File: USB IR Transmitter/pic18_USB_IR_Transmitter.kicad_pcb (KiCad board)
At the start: 2 copper layers, 50.8 x 25.4 mm, 26 parts, among them CON1 USB-MINI-B, P1 CONN_6, P2 CONN_4, P3 CONN_6, P4 CONN_6, P5 CONN_4, P6 CONN_1, P7 CONN_8, Q1 2N7002, U1 1586-PIC18F4550-I/PT, X1 12Mhz

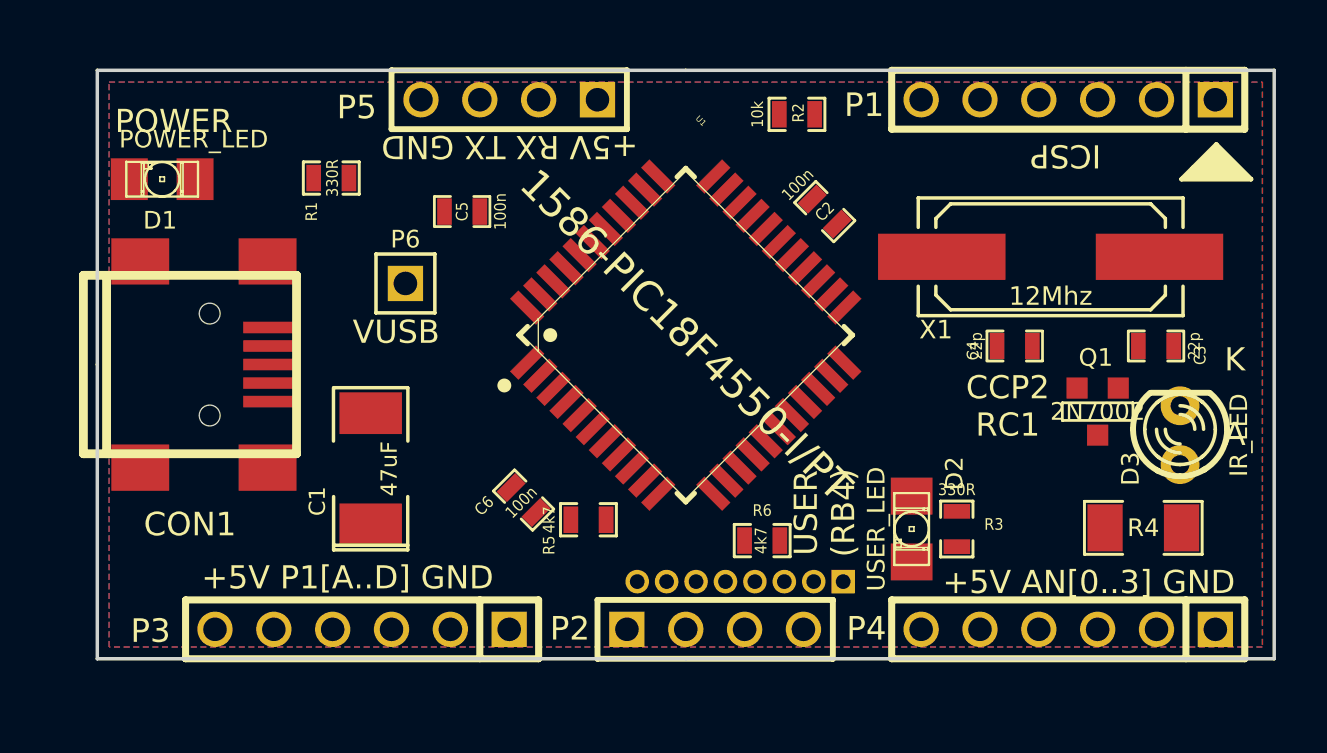
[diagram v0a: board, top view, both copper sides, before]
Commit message: fixed footprint name error in PIC18f board, rerouted board layout
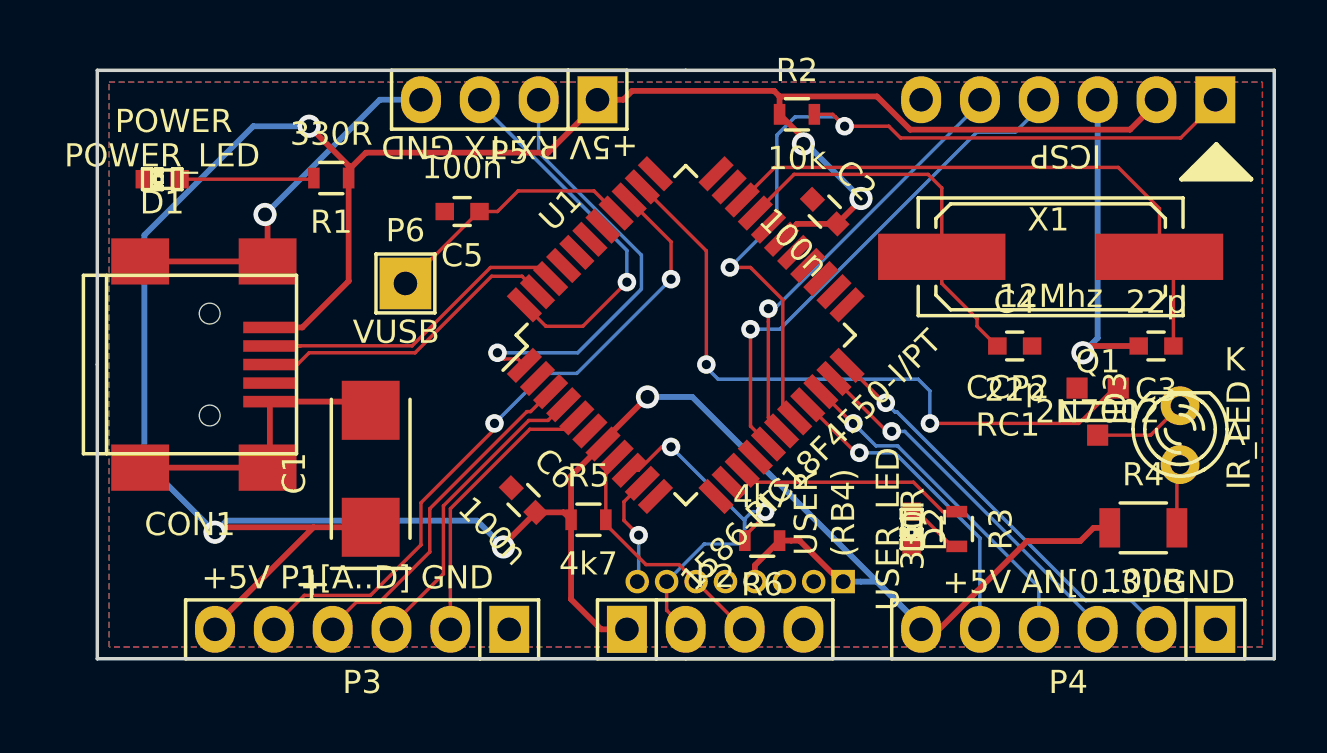
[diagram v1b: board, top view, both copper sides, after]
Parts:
- C1: footprint SM2010 -> Capacitors_Tantalum_SMD:TantalC_SizeC_EIA-6032_Reflow
- C2, C3, C4, C5, C6: footprint SM0603_Capa -> Capacitors_SMD:C_0603
- CON1: footprint USB_MINI_B -> Connect:USB_Mini-B
- D1, D2: footprint LED-1206 -> LEDs:LED-0603
- D3: footprint LED-3MM -> LEDs:LED-3MM
- P1: footprint PIN_ARRAY-6X1 -> Pin_Headers:Pin_Header_Angled_1x06; moved to B.Cu
- P2, P5: footprint PIN_ARRAY_4x1 -> Pin_Headers:Pin_Header_Straight_1x04
- P3, P4: footprint PIN_ARRAY-6X1 -> Pin_Headers:Pin_Header_Straight_1x06
- P6: footprint PIN_ARRAY_1 -> Pin_Headers:Pin_Header_Straight_1x01
- P7: footprint pin_array_8_50mil -> midas_lcd:midas_i2c_lcd
- Q1: footprint SOT23GDS -> SMD_Packages:SOT-23-GDS
- R1, R2, R3, R5, R6: footprint SM0603_Resistor -> Resistors_SMD:R_0603
- R4: footprint SM1206 -> Resistors_SMD:R_1206
- U1: footprint axylf: -> QFP:LQFP-44_10x10mm_Pitch0.8mm
- X1: footprint Q_49U3HMS -> Crystals_Oscillators_SMD:Q_49U3HMS
- turned U1 to 45 degrees
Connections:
- CON1 pad 4: (no net) -> Net-(CON1-Pad4)
- P1 pad 6: (no net) -> Net-(P1-Pad6)
- P7 pad 2: (no net) -> Net-(P7-Pad2)
- P7 pad 3: (no net) -> Net-(P7-Pad3)
- U1 pad 11: (no net) -> Net-(U1-Pad11)
- U1 pad 12: (no net) -> Net-(U1-Pad12)
- U1 pad 13: (no net) -> Net-(U1-Pad13)
- U1 pad 15: (no net) -> Net-(U1-Pad15)
- U1 pad 2: (no net) -> Net-(U1-Pad2)
- U1 pad 23: (no net) -> Net-(U1-Pad23)
- U1 pad 24: (no net) -> Net-(U1-Pad24)
- U1 pad 25: (no net) -> Net-(U1-Pad25)
- U1 pad 26: (no net) -> Net-(U1-Pad26)
- U1 pad 27: (no net) -> Net-(U1-Pad27)
- U1 pad 32: (no net) -> Net-(U1-Pad32)
- U1 pad 33: (no net) -> Net-(U1-Pad33)
- U1 pad 34: (no net) -> Net-(U1-Pad34)
- U1 pad 38: (no net) -> Net-(U1-Pad38)
- U1 pad 39: (no net) -> Net-(U1-Pad39)
- U1 pad 40: (no net) -> Net-(U1-Pad40)
- U1 pad 41: (no net) -> Net-(U1-Pad41)
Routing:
- net +5V: track 0.00 -> 162.4 mm, vias 0 -> 6
- net GND: track 0.00 -> 43.0 mm, vias 0 -> 2
- net ~MCLR~: track 0.00 -> 36.6 mm, vias 0 -> 2
- net IR_LED: track 0.00 -> 29.2 mm, vias 0 -> 2
- net P1A: track 0.00 -> 28.9 mm, vias 0 -> 2
- net /OSC2: track 0.00 -> 25.5 mm
- net PGD: track 0.00 -> 22.1 mm, vias 0 -> 1
- net /RX: track 0.00 -> 18.8 mm, vias 0 -> 1
- net PGC: track 0.00 -> 18.5 mm, vias 0 -> 1
- net /AN3: track 0.00 -> 18.2 mm, vias 0 -> 1
- net SCL: track 0.00 -> 17.9 mm, vias 0 -> 2
- net /OSC1: track 0.00 -> 16.8 mm
- net /TX: track 0.00 -> 16.1 mm, vias 0 -> 1
- net /AN2: track 0.00 -> 16.0 mm, vias 0 -> 1
- net P1B: track 0.00 -> 14.8 mm
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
